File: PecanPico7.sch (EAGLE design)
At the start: 172 parts, among them IC1 Si4464-B1B-FM, IC10 TC1185-1.8VCT713, IC11 TC1185-2.5VCT713, IC12 ADR380ARTZ, IC13 RF6886, IC14 ALM-GP003, IC15 MPU-9250, IC16 PAC1720-1-AIA-TR, IC2 Si4464-B1B-FM, IC3 BME280_BME280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

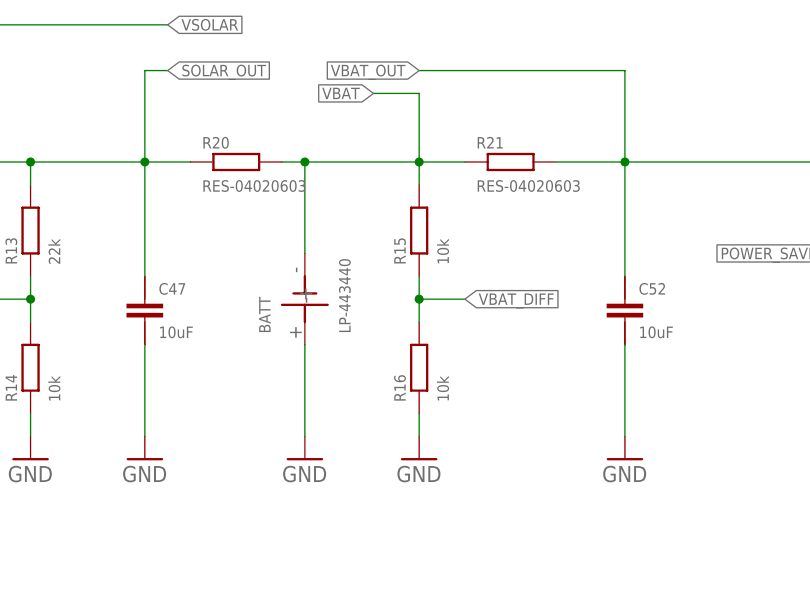
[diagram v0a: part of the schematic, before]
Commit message: Added switching SJ to battery
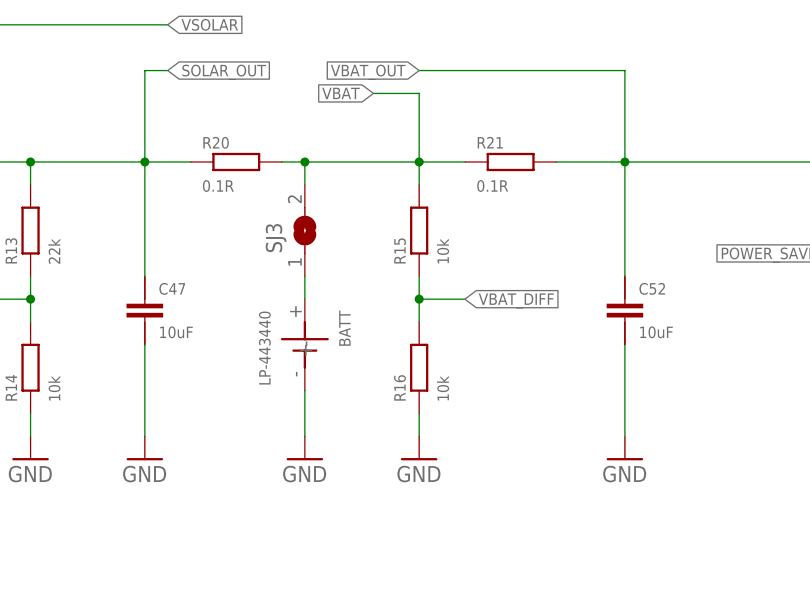
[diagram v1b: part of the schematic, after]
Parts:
- added SJ3: (no value), PecanPico6:SJ
- R20, R21: value RES-04020603 -> 0.1R
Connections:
- new net N$14: BATT.+, SJ3.1
- net GND: now also BATT.-; no longer BATT.+
- net VBAT: now also SJ3.2; no longer BATT.-
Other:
- moved on the sheet: BATT
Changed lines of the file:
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@@
 <part name="SJ2" library="PecanPico6" deviceset="SJ" device=""/>
 <part name="R43" library="sven" deviceset="RES-0402" device="0805" value="0R"/>
-<part name="R20" library="sven" deviceset="RES-0402" device="0603" value="RES-04020603"/>
-<part name="R21" library="sven" deviceset="RES-0402" device="0603" value="RES-04020603"/>
+<part name="R20" library="sven" deviceset="RES-0402" device="0603" value="0.1R"/>
+<part name="R21" library="sven" deviceset="RES-0402" device="0603" value="0.1R"/>
+<part name="SJ3" library="PecanPico6" deviceset="SJ" device=""/>
 </parts>
 <sheets>
@@
 <instance part="C57" gate="G$1" x="-106.68" y="190.5"/>
 <instance part="GND79" gate="1" x="-106.68" y="175.26"/>
-<instance part="BATT" gate="G$1" x="-129.54" y="391.16" rot="R90"/>
+<instance part="BATT" gate="G$1" x="-129.54" y="386.08" rot="R270"/>
 <instance part="GND51" gate="1" x="-129.54" y="373.38"/>
 <instance part="X1" gate="-1" x="-114.3" y="152.4"/>
@@
 <instance part="R20" gate="G$1" x="-137.16" y="406.4"/>
 <instance part="R21" gate="G$1" x="-106.68" y="406.4"/>
+<instance part="SJ3" gate="1" x="-129.54" y="398.78" rot="R90"/>
 </instances>
 <busses>
@@
 </segment>
 <segment>
-<pinref part="BATT" gate="G$1" pin="+"/>
-<wire x1="-129.54" y1="386.08" x2="-129.54" y2="375.92" width="0.1524" layer="91"/>
-<pinref part="GND51" gate="1" pin="GND"/>
-</segment>
-<segment>
 <pinref part="X1" gate="-15" pin="S"/>
 <wire x1="-116.84" y1="114.3" x2="-134.62" y2="114.3" width="0.1524" layer="91"/>
@@
 <pinref part="GND104" gate="1" pin="GND"/>
 </segment>
+<segment>
+<pinref part="BATT" gate="G$1" pin="-"/>
+<pinref part="GND51" gate="1" pin="GND"/>
+<wire x1="-129.54" y1="381" x2="-129.54" y2="375.92" width="0.1524" layer="91"/>
+</segment>
 </net>
 <net name="N$5" class="0">
@@
 <wire x1="-116.84" y1="406.4" x2="-111.76" y2="406.4" width="0.1524" layer="91"/>
 <wire x1="-116.84" y1="406.4" x2="-116.84" y2="403.86" width="0.1524" layer="91"/>
-<wire x1="-132.08" y1="406.4" x2="-129.54" y2="406.4" width="0.1524" layer="91"/>
 <junction x="-116.84" y="406.4"/>
+<wire x1="-132.08" y1="406.4" x2="-129.54" y2="406.4" width="0.1524" layer="91"/>
 <wire x1="-129.54" y1="406.4" x2="-116.84" y2="406.4" width="0.1524" layer="91"/>
 <wire x1="-116.84" y1="406.4" x2="-116.84" y2="414.02" width="0.1524" layer="91"/>
 <wire x1="-116.84" y1="414.02" x2="-121.92" y2="414.02" width="0.1524" layer="91"/>
 <label x="-121.92" y="414.02" size="1.27" layer="95" rot="R180" xref="yes"/>
-<pinref part="BATT" gate="G$1" pin="-"/>
-<wire x1="-129.54" y1="396.24" x2="-129.54" y2="406.4" width="0.1524" layer="91"/>
-<junction x="-129.54" y="406.4"/>
 <pinref part="R20" gate="G$1" pin="2"/>
 <pinref part="R21" gate="G$1" pin="1"/>
+<pinref part="SJ3" gate="1" pin="2"/>
+<wire x1="-129.54" y1="406.4" x2="-129.54" y2="403.86" width="0.1524" layer="91"/>
+<junction x="-129.54" y="406.4"/>
 </segment>
 <segment>
@@
 </segment>
 </net>
+<net name="N$14" class="0">
+<segment>
+<pinref part="SJ3" gate="1" pin="1"/>
+<pinref part="BATT" gate="G$1" pin="+"/>
+<wire x1="-129.54" y1="393.7" x2="-129.54" y2="391.16" width="0.1524" layer="91"/>
+</segment>
+</net>

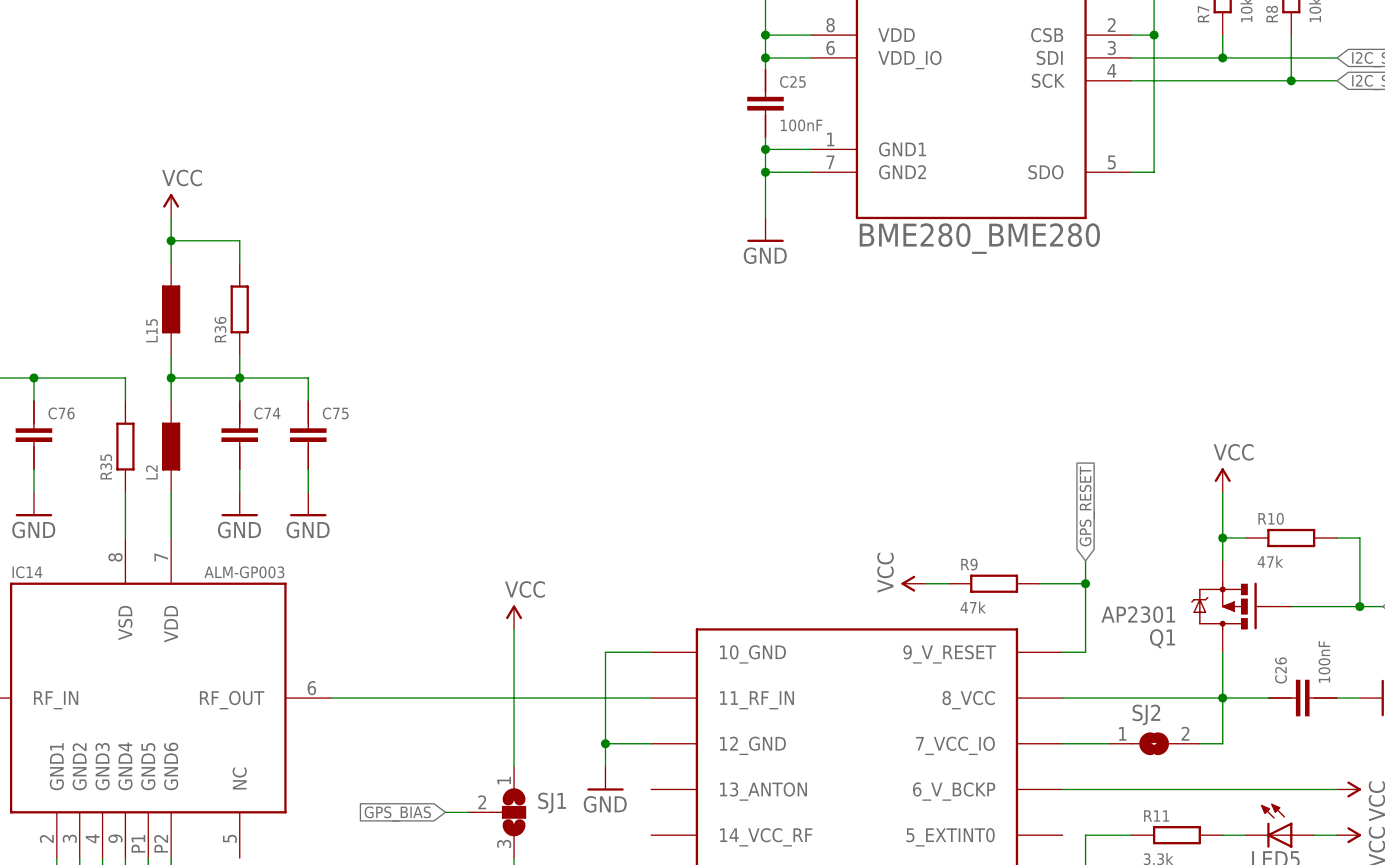
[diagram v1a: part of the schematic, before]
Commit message: Fixed GPS preamp VCC connection
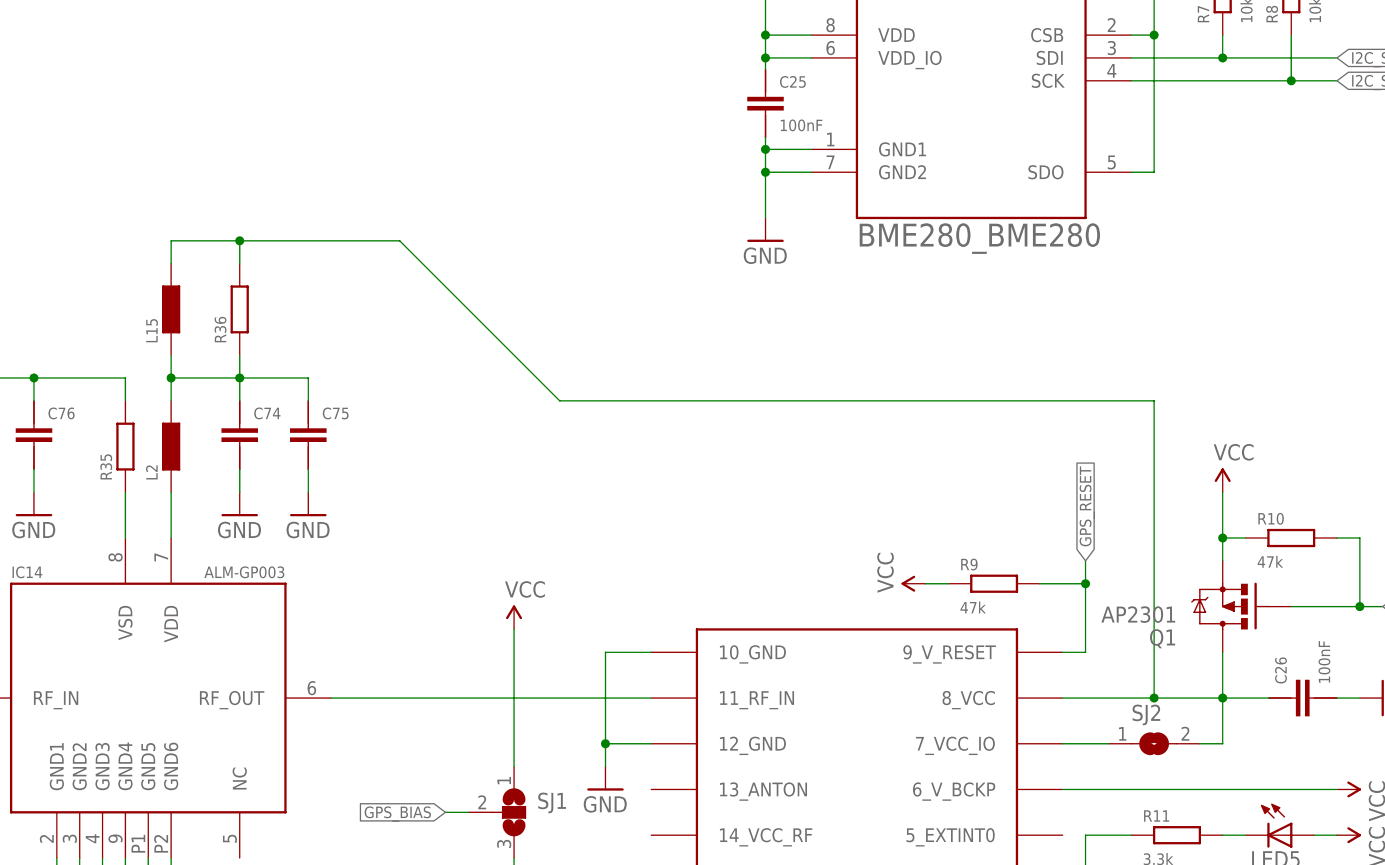
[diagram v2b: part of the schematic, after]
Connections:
- net N$29: now also L15.2, R36.2
- net VCC: no longer L15.2, R36.2
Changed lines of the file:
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@@
 <part name="C74" library="PecanPico6" deviceset="CAP-0402" device="" value=""/>
 <part name="C75" library="PecanPico6" deviceset="CAP-0402" device="" value=""/>
-<part name="P+37" library="PecanPico6" deviceset="3.3V" device="" value="VCC"/>
 <part name="GND96" library="PecanPico6" deviceset="GND" device=""/>
 <part name="GND97" library="PecanPico6" deviceset="GND" device=""/>
@@
 <instance part="C74" gate="G$1" x="109.22" y="429.26"/>
 <instance part="C75" gate="G$1" x="116.84" y="429.26"/>
-<instance part="P+37" gate="G$1" x="101.6" y="452.12"/>
 <instance part="GND96" gate="1" x="109.22" y="419.1"/>
 <instance part="GND97" gate="1" x="116.84" y="419.1"/>
@@
 </segment>
 <segment>
-<pinref part="L15" gate="G$1" pin="2"/>
-<wire x1="101.6" y1="447.04" x2="101.6" y2="449.58" width="0.1524" layer="91"/>
-<pinref part="R36" gate="G$1" pin="2"/>
-<wire x1="109.22" y1="447.04" x2="109.22" y2="449.58" width="0.1524" layer="91"/>
-<wire x1="109.22" y1="449.58" x2="101.6" y2="449.58" width="0.1524" layer="91"/>
-<wire x1="101.6" y1="449.58" x2="101.6" y2="452.12" width="0.1524" layer="91"/>
-<junction x="101.6" y="449.58"/>
-<pinref part="P+37" gate="G$1" pin="VCC"/>
-</segment>
-<segment>
 <pinref part="IC15" gate="G$1" pin="NCS"/>
 <pinref part="P+40" gate="G$1" pin="VCC"/>
@@
 <pinref part="IC4" gate="G$1" pin="8_VCC"/>
 <pinref part="Q1" gate="G$1" pin="D"/>
-<wire x1="200.66" y1="398.78" x2="218.44" y2="398.78" width="0.1524" layer="91"/>
+<wire x1="200.66" y1="398.78" x2="210.82" y2="398.78" width="0.1524" layer="91"/>
+<wire x1="210.82" y1="398.78" x2="218.44" y2="398.78" width="0.1524" layer="91"/>
 <wire x1="218.44" y1="398.78" x2="218.44" y2="403.86" width="0.1524" layer="91"/>
 <wire x1="218.44" y1="398.78" x2="223.52" y2="398.78" width="0.1524" layer="91"/>
@@
 <wire x1="215.9" y1="393.7" x2="218.44" y2="393.7" width="0.1524" layer="91"/>
 <wire x1="218.44" y1="393.7" x2="218.44" y2="398.78" width="0.1524" layer="91"/>
-</segment>
-</net>
+<pinref part="R36" gate="G$1" pin="2"/>
+<wire x1="109.22" y1="447.04" x2="109.22" y2="449.58" width="0.1524" layer="91"/>
+<wire x1="109.22" y1="449.58" x2="127" y2="449.58" width="0.1524" layer="91"/>
+<wire x1="127" y1="449.58" x2="144.78" y2="431.8" width="0.1524" layer="91"/>
+<wire x1="144.78" y1="431.8" x2="210.82" y2="431.8" width="0.1524" layer="91"/>
+<wire x1="210.82" y1="431.8" x2="210.82" y2="398.78" width="0.1524" layer="91"/>
+<junction x="210.82" y="398.78"/>
+<pinref part="L15" gate="G$1" pin="2"/>
+<wire x1="101.6" y1="447.04" x2="101.6" y2="449.58" width="0.1524" layer="91"/>
+<wire x1="101.6" y1="449.58" x2="109.22" y2="449.58" width="0.1524" layer="91"/>
+<junction x="109.22" y="449.58"/>
+</segment>
+</net>

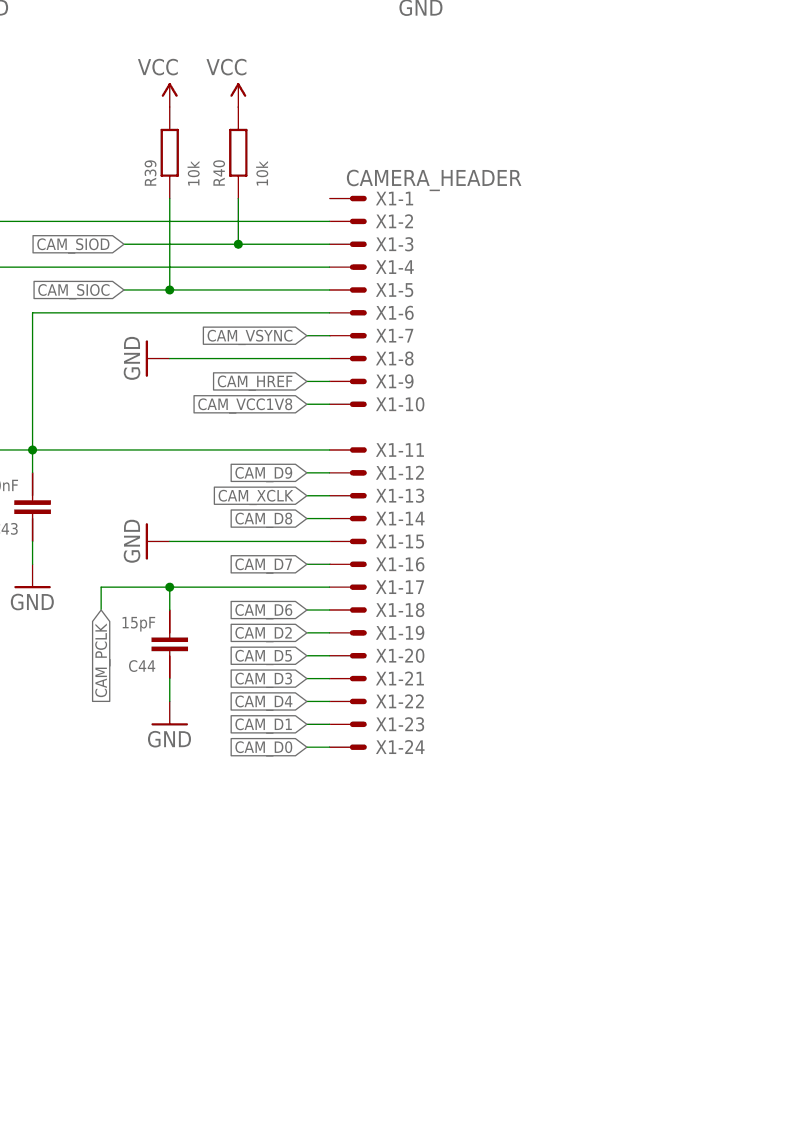
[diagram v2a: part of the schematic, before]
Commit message: Improved GND connections
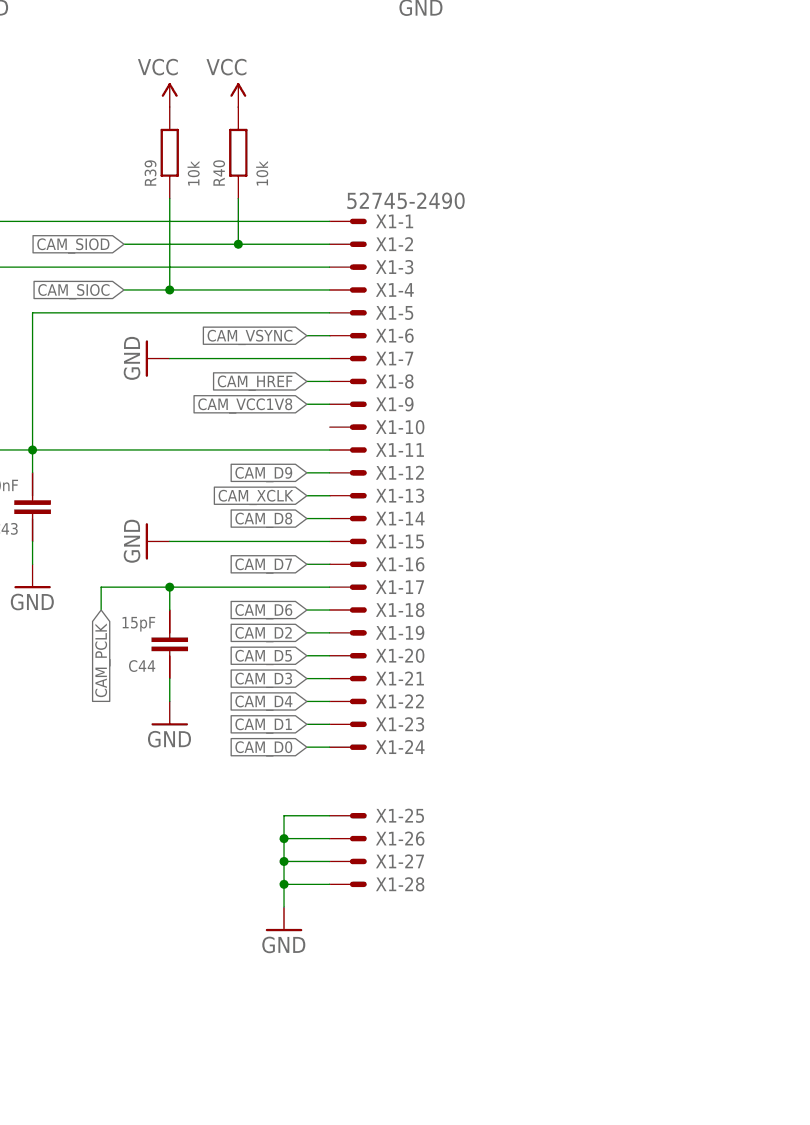
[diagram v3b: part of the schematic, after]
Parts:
- X1: value CAMERA_HEADER -> 52745-2490
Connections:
- net AGND: now also X1-1.S; no longer X1-2.S
- net CAM_HREF: now also X1-8.S; no longer X1-9.S
- net CAM_SIOC: now also X1-4.S; no longer X1-5.S
- net CAM_SIOD: now also X1-2.S; no longer X1-3.S
- net CAM_VCC1V8: now also X1-9.S; no longer X1-10.S
- net CAM_VCC2V5: now also X1-3.S; no longer X1-4.S
- net CAM_VCC3V0: now also X1-5.S; no longer X1-6.S
- net CAM_VSYNC: now also X1-6.S; no longer X1-7.S
- net GND: now also X1-25.S, X1-26.S, X1-27.S, X1-28.S, X1-7.S; no longer X1-8.S
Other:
- moved on the sheet: X1-1, X1-10, X1-2, X1-3, X1-4, X1-5, X1-6, X1-7, X1-8, X1-9

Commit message: Done many things Added solar GND pads Added names to components Done on-board documentation
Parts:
- added JP4: (no value), SparkFun-Connectors:M01PTH
- added JP5, JP6, JP7: (no value), SparkFun-Connectors:M01SMD
- R2, R3, R5, R6: value 10k -> 1k
- R32, R33, R34: value 3.3k -> 1k
- renumbered IC14 to IC6, IC8 to TCXO
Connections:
- net GND: now also JP4.1, JP5.1, JP6.1, JP7.1
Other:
- note added: "GPSRX"
- note added: "MANAGEMENT"
- note added: "RADIO1"
- note added: "RADIO2"
- note added: "RWR"
- moved on the sheet: JP1, JP2

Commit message: Fixed camera connection, tidy up
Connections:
- net AGND: now also X1-2.S; no longer X1-1.S
- net CAM_HREF: now also X1-9.S; no longer X1-8.S
- net CAM_SIOC: now also X1-5.S; no longer X1-4.S
- net CAM_SIOD: now also X1-3.S; no longer X1-2.S
- net CAM_VCC1V8: now also X1-10.S; no longer X1-9.S
- net CAM_VCC2V5: now also X1-4.S; no longer X1-3.S
- net CAM_VCC3V0: now also X1-6.S; no longer X1-5.S
- net CAM_VSYNC: now also X1-7.S; no longer X1-6.S
- net GND: now also X1-8.S; no longer X1-7.S
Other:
- note added: "- External connections - I2C on top (to connect another BME280 for measuring ballon pressure) - UART for debugging - 2 additional GPIOs - 4 Status LEDs for debugging - 1 LED connected to GPS timepulse - Both radios have 2 debug LEDs each - TCXO 26MHz for Si-Chips of STM32 - The PCB has the size of a battery which perfectly fits on the back of the PCB and which we've tested already at -40°C (BAK L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"
- note added: "- STM32F429IIH6 (max. 180MHz, 2MB Flash, 256kB SRAM) - uBlox MAX7 with preamp and pre-filtering - Camera OV2640 (2MB) - Radio A (Si4060) with PA (RF6886 2...5W) FSK and APRS capable, TX only, 2m LPF (I did this in order to communicate with satellites) - Radio B (Si406x) RX/TX 10mW or TX only 100mW FSK and APRS capable, 2m or 70cm LPF - BME280 Sensor (airpressure, humidity, temperature) - MPU9250 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"
- note added: "ADC"
- note added: "AF5LI KT5TK"
- note added: "CAM"
- note added: "CLOCK"
- note added: "DL7AD DL4MDW"
- note added: "Features"
- note added: "GPS"
- note added: "Input Output"
- note added: "LED"
- note added: "MPU"
- note added: "POWER MANAGEMENT"
- note added: "Pecan Pico 7 - APRS Camera Tracker"
- note added: "RADIOS"
- note added: "SD"
- note added: "SENSING"
- note added: "SPI / I2C"
- note added: "SWD"
- note added: "Sven Steudte Thomas Krahn"
- note added: "UART"
- note removed: "CAMERA"
- note removed: "COM"
- moved on the sheet: C1, C10, C11, C12, C13, C14, C15, C16, C17, C18, C19, C2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
